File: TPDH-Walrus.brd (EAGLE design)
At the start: 16 x 39.9 mm, 44 parts, among them Q2 DMG3404, U1 MS5803-14BA, U2 SN65HVD33RHL, U4 MCP3421A3, U5 TPS79733, U6 MAX6070AAUT18, U7 TXS0102DQM

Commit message: 1 via, lots of work
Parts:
- moved C3 0.18 mm to (14.4, 29.4)
- moved C9 0.18 mm to (14.4, 27.2)
- moved U5 0.18 mm to (13.7, 23.3)
- moved R1 0.18 mm to (13.0, 31.6)
- moved C1 0.18 mm to (14.4, 25.0), turned to 0 degrees
- moved C10 0.18 mm to (14.4, 26.1)
- moved C8 0.18 mm to (14.4, 28.3)
- moved R5 0.18 mm to (14.4, 30.5)
- moved R3 0.13 mm to (11.3, 27.3)
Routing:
- net +3V3: track 81.6 -> 79.0 mm, vias 9 -> 8
- net GND: track 77.9 -> 79.1 mm

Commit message: Cable solder ring silk
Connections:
- net N$1 renamed SPI-I2C-SWITCH
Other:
- board text added: "I2C <3 m"
- board text added: "RS485: <1000 m"
- board text added: "Rx+"
- board text added: "Rx-"
- board text added: "SCL"
- board text added: "SDA"
- board text added: "Tx+"
- board text added: "Tx-"
- board text added: "V+"
- board text added: "V-"
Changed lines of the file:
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@@
 <setting verticaltext="up"/>
 </settings>
-<grid distance="5" unitdist="mil" unit="mil" style="lines" multiple="1" display="no" altdistance="1" altunitdist="mm" altunit="mm"/>
+<grid distance="0.1" unitdist="mm" unit="mm" style="lines" multiple="1" display="no" altdistance="1" altunitdist="mm" altunit="mm"/>
 <layers>
 <layer number="1" name="Top" color="4" fill="1" visible="yes" active="yes"/>
@@
 <layer number="18" name="Vias" color="2" fill="1" visible="yes" active="yes"/>
 <layer number="19" name="Unrouted" color="6" fill="1" visible="yes" active="yes"/>
-<layer number="20" name="Dimension" color="15" fill="1" visible="yes" active="yes"/>
-<layer number="21" name="tPlace" color="7" fill="1" visible="yes" active="yes"/>
-<layer number="22" name="bPlace" color="7" fill="1" visible="yes" active="yes"/>
+<layer number="20" name="Dimension" color="15" fill="1" visible="no" active="yes"/>
+<layer number="21" name="tPlace" color="7" fill="1" visible="no" active="yes"/>
+<layer number="22" name="bPlace" color="7" fill="1" visible="no" active="yes"/>
 <layer number="23" name="tOrigins" color="15" fill="1" visible="yes" active="yes"/>
 <layer number="24" name="bOrigins" color="15" fill="1" visible="yes" active="yes"/>
-<layer number="25" name="tNames" color="7" fill="1" visible="yes" active="yes"/>
-<layer number="26" name="bNames" color="7" fill="1" visible="yes" active="yes"/>
-<layer number="27" name="tValues" color="7" fill="1" visible="yes" active="yes"/>
-<layer number="28" name="bValues" color="7" fill="1" visible="yes" active="yes"/>
+<layer number="25" name="tNames" color="7" fill="1" visible="no" active="yes"/>
+<layer number="26" name="bNames" color="7" fill="1" visible="no" active="yes"/>
+<layer number="27" name="tValues" color="7" fill="1" visible="no" active="yes"/>
+<layer number="28" name="bValues" color="7" fill="1" visible="no" active="yes"/>
 <layer number="29" name="tStop" color="7" fill="3" visible="no" active="yes"/>
 <layer number="30" name="bStop" color="7" fill="6" visible="no" active="yes"/>
@@
 <layer number="116" name="Patch_BOT" color="9" fill="4" visible="no" active="yes"/>
 <layer number="118" name="Rect_Pads" color="7" fill="1" visible="no" active="yes"/>
-<layer number="121" name="_tsilk" color="7" fill="1" visible="no" active="yes"/>
-<layer number="122" name="_bsilk" color="7" fill="1" visible="no" active="yes"/>
+<layer number="121" name="_tsilk" color="7" fill="1" visible="yes" active="yes"/>
+<layer number="122" name="_bsilk" color="7" fill="1" visible="yes" active="yes"/>
 <layer number="123" name="tTestmark" color="7" fill="1" visible="no" active="yes"/>
 <layer number="124" name="bTestmark" color="7" fill="1" visible="no" active="yes"/>
@@
 <wire x1="0" y1="2" x2="2" y2="0" width="0" layer="20" curve="90"/>
 <wire x1="14" y1="0" x2="16" y2="2" width="0" layer="20" curve="90"/>
+<text x="3.256" y="7.112" size="0.6" layer="52" rot="MR0">V-</text>
+<text x="5.7" y="7.112" size="0.6" layer="52" rot="MR0">Tx+</text>
+<text x="7.6" y="7.112" size="0.6" layer="52" rot="MR0">Tx-</text>
+<text x="9.556" y="7.112" size="0.6" layer="52" rot="MR0">Rx-</text>
+<text x="11.556" y="7.112" size="0.6" layer="52" rot="MR0">Rx+</text>
+<text x="13.456" y="7.112" size="0.6" layer="52" rot="MR0">V+</text>
+<text x="5.856" y="11.112" size="0.6" layer="52" rot="MR0">SCL</text>
+<text x="7.956" y="11.112" size="0.6" layer="52" rot="MR0">SDA</text>
+<text x="9.456" y="11.112" size="0.6" layer="52" rot="MR0">V-</text>
+<text x="11.456" y="11.112" size="0.6" layer="52" rot="MR0">V+</text>
+<text x="14.156" y="9.112" size="0.6" layer="52" rot="MR0">I2C
+&lt;3 m</text>
+<text x="10.956" y="4.012" size="0.6" layer="52" rot="MR0">RS485: &lt;1000 m</text>
 </plain>
 <attributes>
@@
 <wire x1="10.5212875" y1="11.1247" x2="9.3655875" y2="9.969" width="0.4064" layer="16"/>
 </signal>
-<signal name="N$1">
+<signal name="SPI-I2C-SWITCH">
 <contactref element="U1" pad="3"/>
 <contactref element="JP1" pad="2"/>
@@
 </drawing>
 <compatibility>
+<note version="6.3" minversion="6.2.2" severity="warning">
+Since Version 6.2.2 text objects can contain more than one line,
+which will not be processed correctly with this version.
+</note>
 <note version="8.2" severity="warning">
 Since Version 8.2, EAGLE supports online libraries. The ids

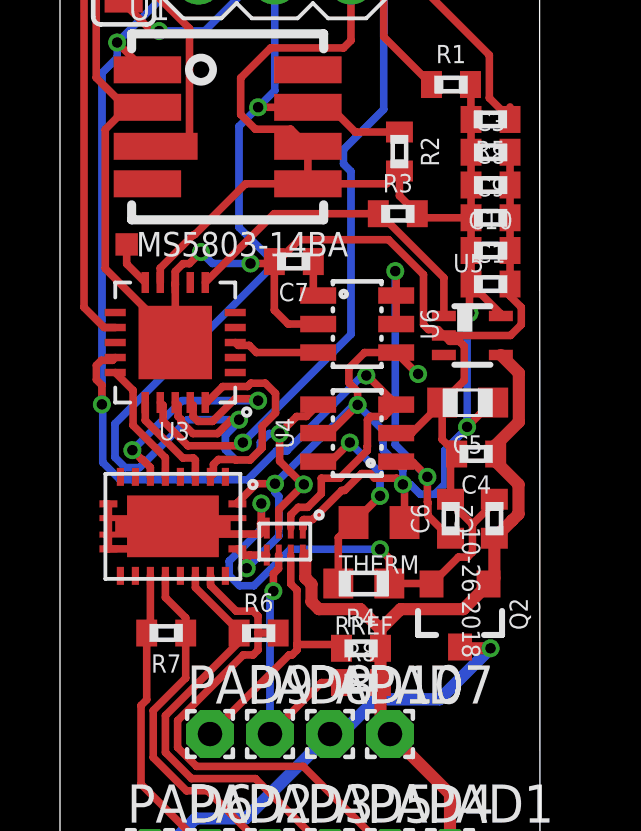
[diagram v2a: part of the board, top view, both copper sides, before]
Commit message: Minor fixes for DRC
Changed power path very slightly, also changed to 0.2mm traces for TSX0102 to avoid clearance issues
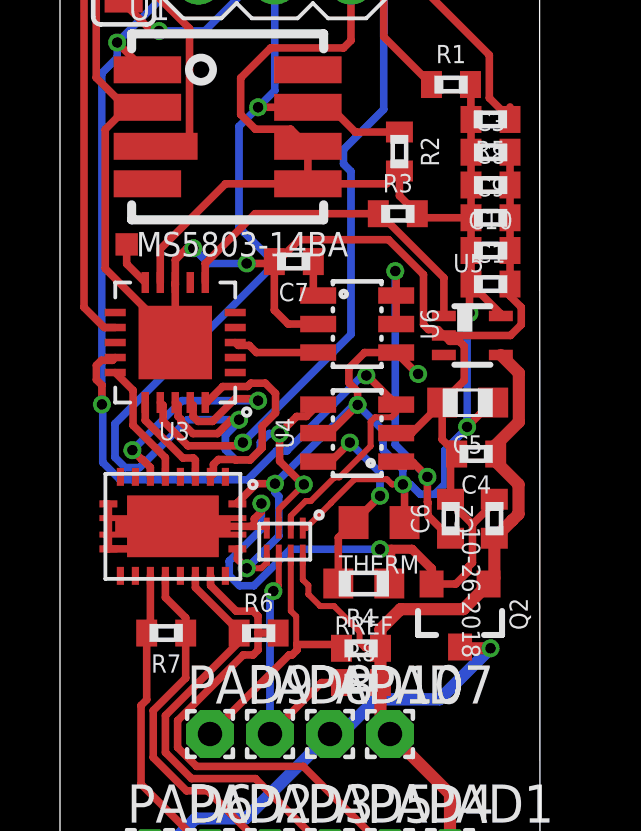
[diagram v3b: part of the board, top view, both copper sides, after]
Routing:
- net GND: track 79.1 -> 80.8 mm

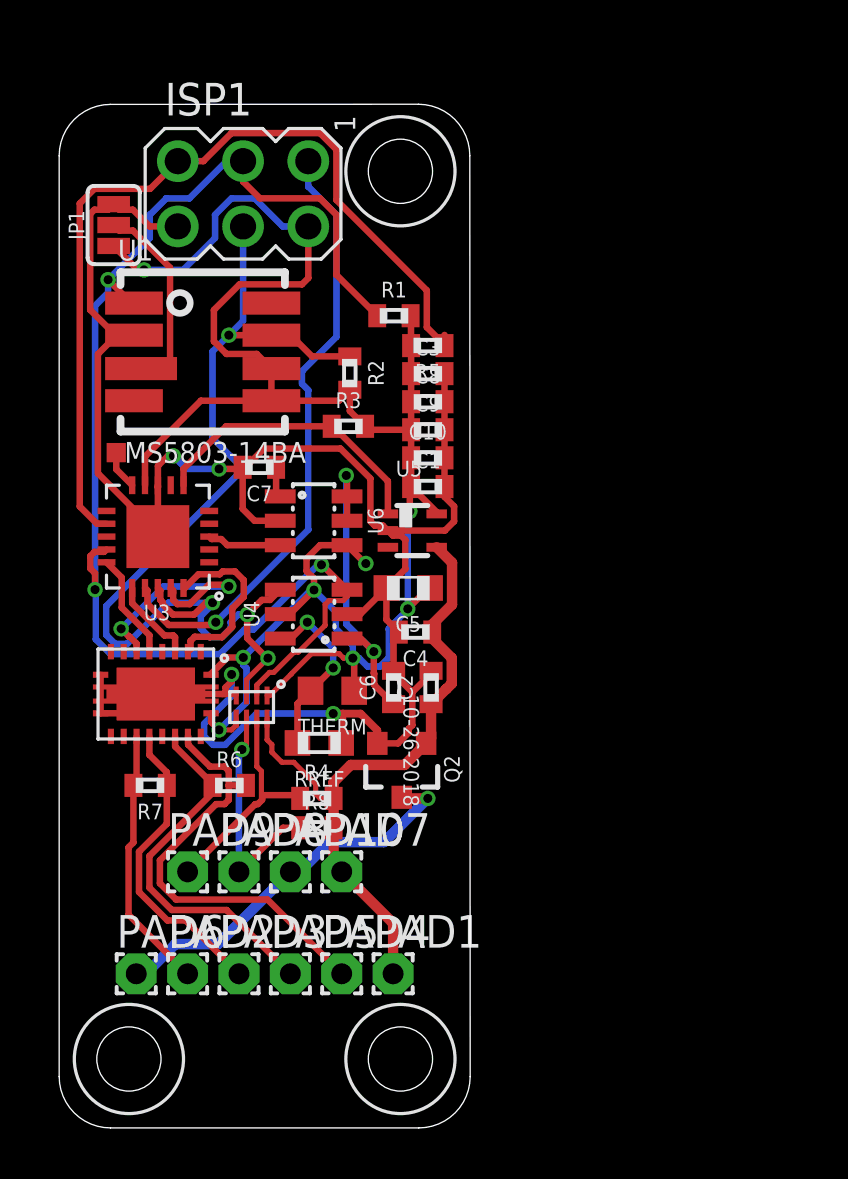
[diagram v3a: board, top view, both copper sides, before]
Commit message: Major revision Add 10 uF cap Reroute to keep decoupling caps near ICs Change schematic to reflect the above reorganization Reroute to move thermistor to upper right
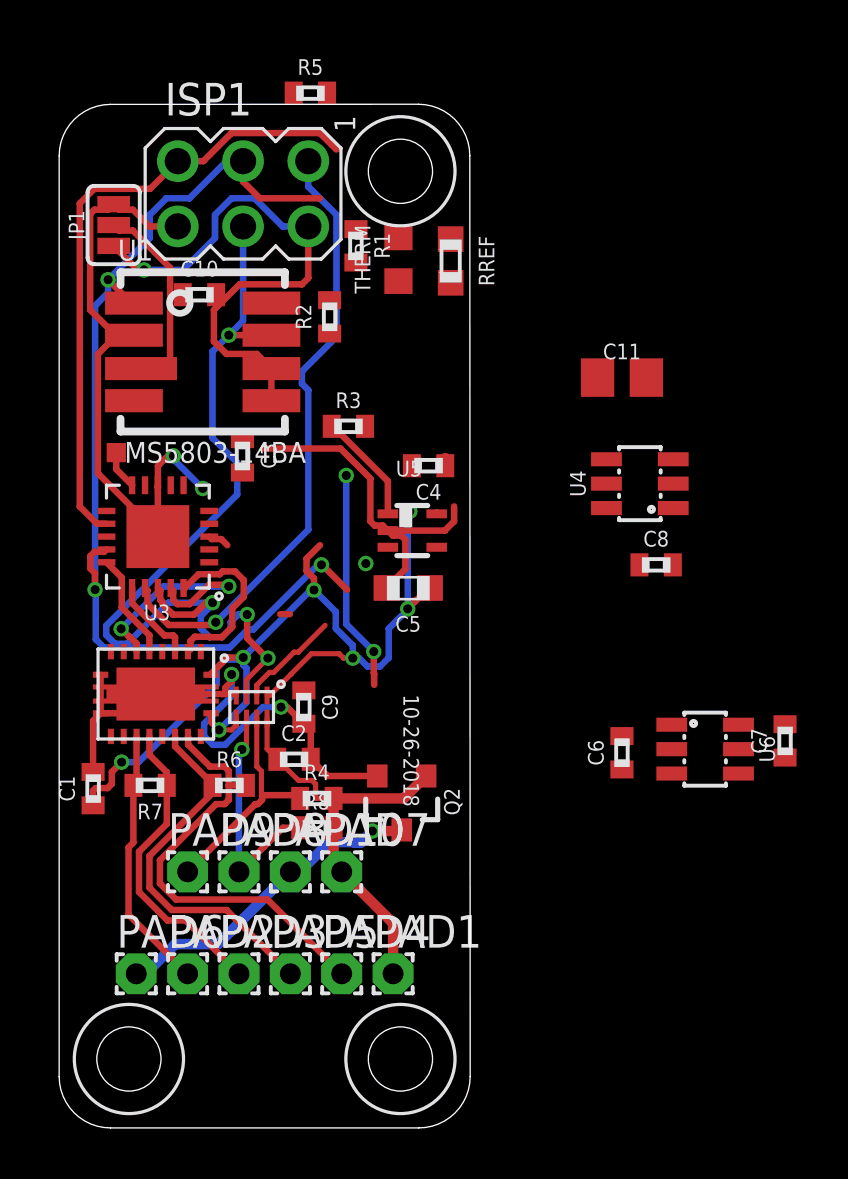
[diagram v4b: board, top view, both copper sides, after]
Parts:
- added C11: 10uF, bschulz:C0805
- moved C7 23.1 mm to (28.3, 15.1), turned to 90 degrees
- moved RREF 19.4 mm to (15.2, 33.7), turned to 270 degrees
- moved U6 17.6 mm to (25.1, 14.7)
- moved C1 17.6 mm to (1.32, 13.2), turned to 90 degrees
- moved THERM 17.0 mm to (13.2, 33.8), turned to 90 degrees
- moved U4 13.7 mm to (22.6, 25.1)
- moved C9 11.8 mm to (9.53, 16.4), turned to 270 degrees
- moved C10 10.9 mm to (5.46, 32.4)
- moved C8 10.9 mm to (23.2, 21.9)
- moved R5 10.8 mm to (9.78, 40.3), turned to 0 degrees
- moved C6 9.25 mm to (21.9, 14.6)
- moved C3 7.89 mm to (7.14, 26.2), turned to 270 degrees
- moved C4 6.50 mm to (14.4, 25.8)
- moved C2 6.02 mm to (9.14, 14.4), turned to 0 degrees
- moved R1 3.10 mm to (11.6, 34.3), turned to 270 degrees
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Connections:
- net +3V3: now also C11.1
- net GND: now also C11.2
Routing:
- net +3V3: track 79.3 -> 60.3 mm, vias 8 -> 9
- net GND: track 80.8 -> 61.8 mm
- net /RESET: track 34.3 -> 24.5 mm
- net VIN+: track 26.4 -> 16.9 mm
- net SCL: track 52.9 -> 45.2 mm
- net PG: track 11.4 -> 4.34 mm
- net VTHERM-: track 7.02 -> 0.00 mm, vias 2 -> 0
- net SDA: track 41.1 -> 36.9 mm
- net VREF: track 12.7 -> 8.64 mm
- net VIN-: track 15.2 -> 12.7 mm
- net REF_EN: track 2.90 -> 0.84 mm
- net N$11: track 1.23 -> 0.18 mm

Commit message: Vin complete
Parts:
- moved C4 10.8 mm to (13.7, 15.0)
- moved R3 9.09 mm to (13.6, 18.5), turned to 180 degrees
- moved U5 6.48 mm to (13.7, 16.8)
- moved C5 5.25 mm to (11.1, 16.4), turned to 270 degrees
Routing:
- net GND: track 61.8 -> 52.7 mm
- net +3V3: track 60.3 -> 54.5 mm, vias 9 -> 6
- net VREF: track 8.64 -> 5.83 mm, vias 2 -> 1
- net VIN+: track 16.9 -> 19.2 mm
- net PG: track 4.34 -> 4.85 mm

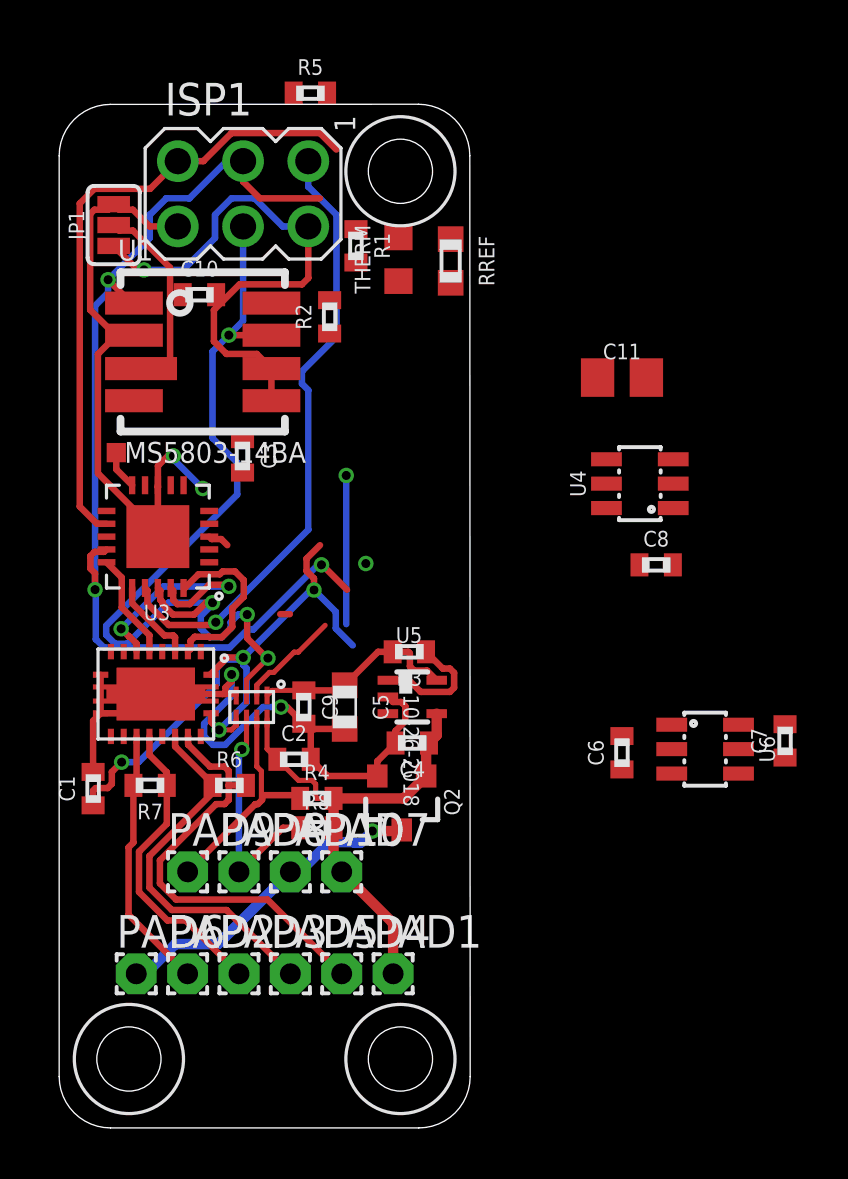
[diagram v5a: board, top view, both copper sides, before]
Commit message: Thermistor passives placed
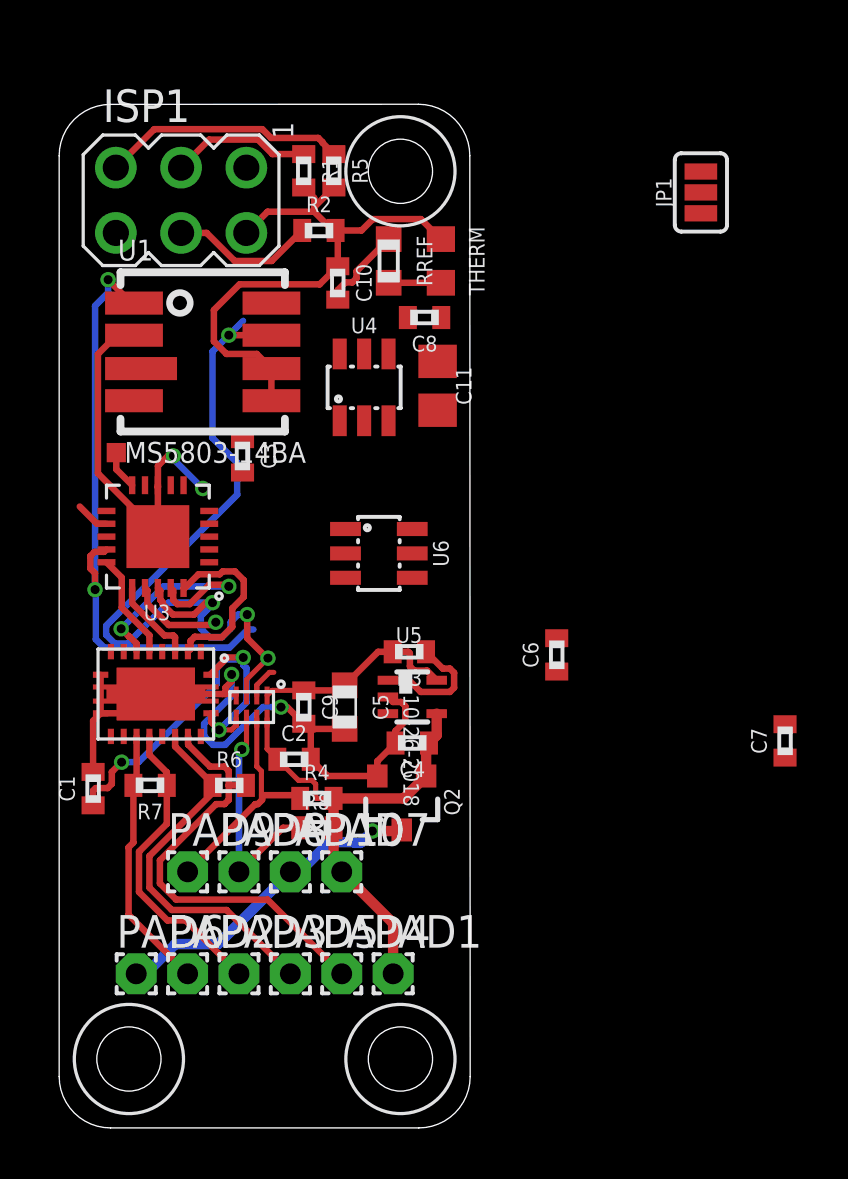
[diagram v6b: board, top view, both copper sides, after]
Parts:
- moved JP1 22.9 mm to (25.0, 36.4)
- moved U6 14.8 mm to (12.4, 22.4)
- moved C8 13.2 mm to (14.2, 31.5), turned to 180 degrees
- moved U4 11.4 mm to (11.9, 28.8), turned to 0 degrees
- moved C11 7.19 mm to (14.7, 28.9), turned to 270 degrees
- moved C10 5.40 mm to (10.8, 32.9), turned to 270 degrees
- moved C6 4.58 mm to (19.4, 18.4)
- moved R1 3.56 mm to (9.52, 37.3)
- moved R2 3.39 mm to (10.1, 34.9), turned to 0 degrees
- moved R5 3.16 mm to (10.7, 37.3), turned to 270 degrees
- moved ISP1 2.43 mm to (4.75, 36.1)
- moved RREF 2.41 mm to (12.8, 33.8)
- moved THERM 1.65 mm to (14.9, 33.8), turned to 270 degrees
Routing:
- net MISO: track 24.3 -> 3.70 mm
- net SCL: track 45.2 -> 31.0 mm, vias 3 -> 2
- net /RESET: track 24.5 -> 10.8 mm
- net +3V3: track 54.5 -> 46.9 mm, vias 6 -> 3
- net SPI-I2C-SWITCH: track 8.04 -> 1.13 mm
- net GND: track 52.7 -> 46.3 mm
- net VREF: track 5.83 -> 0.00 mm, vias 1 -> 0
- net VTHERM-: track 0.00 -> 2.03 mm
- net SDA: track 36.9 -> 38.9 mm
- net REF_EN: track 0.84 -> 0.00 mm

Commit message: Thermistor ICs
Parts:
- moved C7 20.5 mm to (11.0, 26.2), turned to 0 degrees
- moved C6 9.25 mm to (14.2, 26.1), turned to 0 degrees
- moved U6 2.34 mm to (10.7, 23.9)
- moved C3 0.89 mm to (8.03, 26.2)
- moved C11 0.63 mm to (14.2, 28.5)
- moved C8 0.55 mm to (14.5, 31.1), turned to 0 degrees
- moved RREF 0.51 mm to (12.3, 33.8)
- moved THERM 0.51 mm to (14.4, 33.8)
- moved R2 0.38 mm to (9.73, 34.9)
- moved U4 0.36 mm to (11.6, 29.1)
- moved C10 0.28 mm to (10.7, 32.6)
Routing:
- net GND: track 46.3 -> 65.7 mm
- net SDA: track 38.9 -> 31.5 mm, vias 4 -> 3
- net VREF: track 0.00 -> 6.63 mm
- net VTHERM-: track 2.03 -> 5.42 mm
- net +3V3: track 46.9 -> 45.1 mm
- net N$11: track 0.00 -> 1.79 mm
